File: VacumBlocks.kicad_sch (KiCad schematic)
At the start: 8 parts, among them M1 Motor_Servo, M2 Motor_Servo, M4 Motor_Servo, U2 Nodemcu-32S

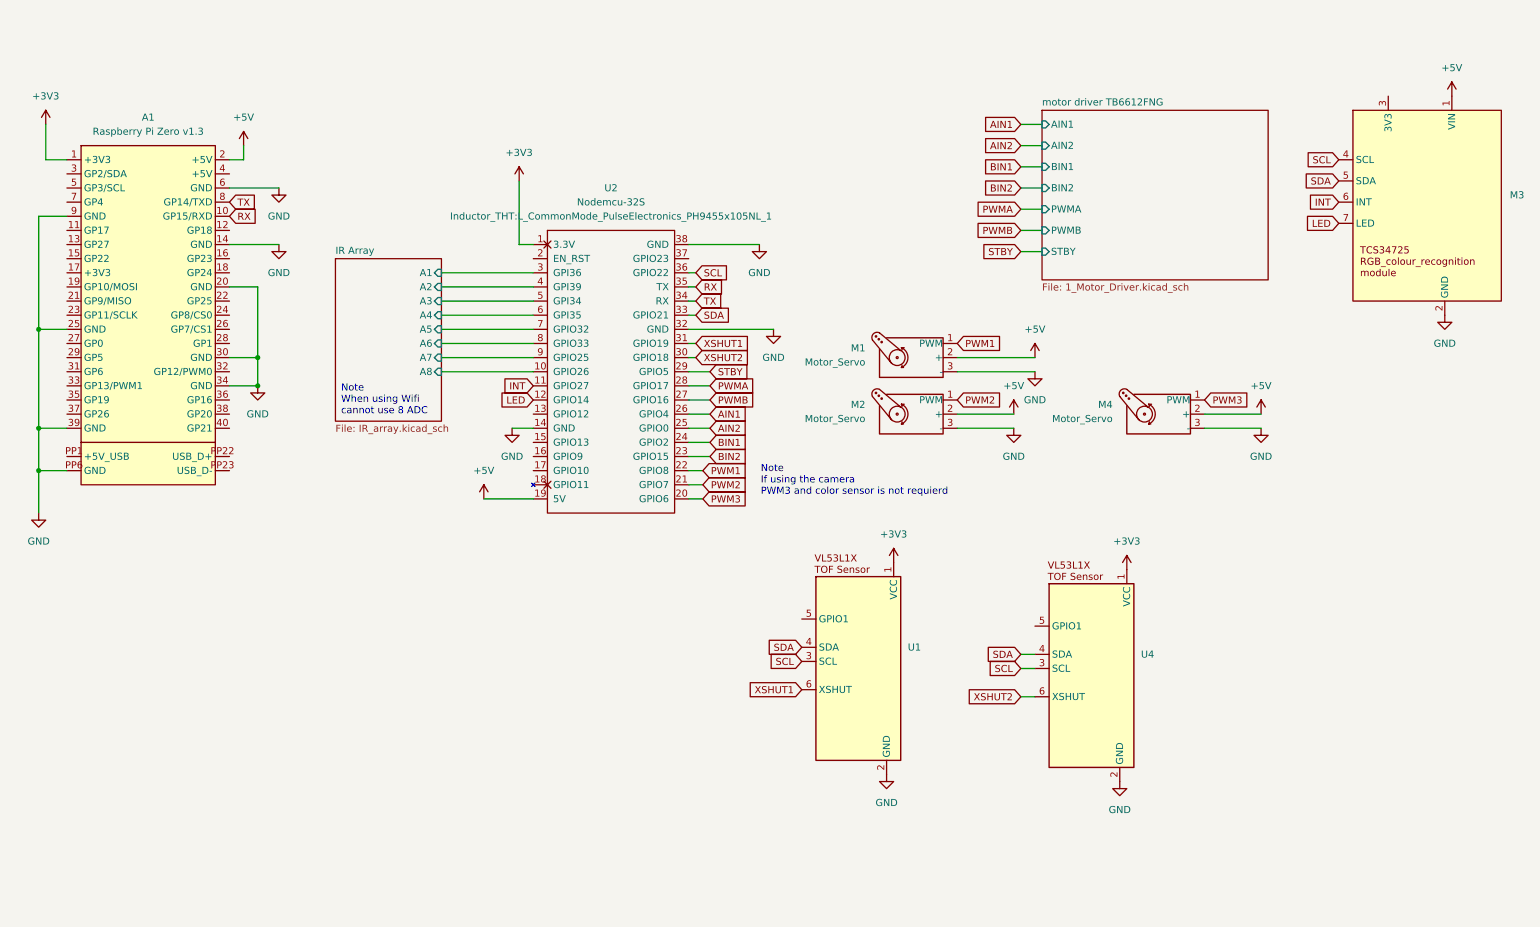
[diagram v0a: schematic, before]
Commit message: Finalized Scematics and Footprint
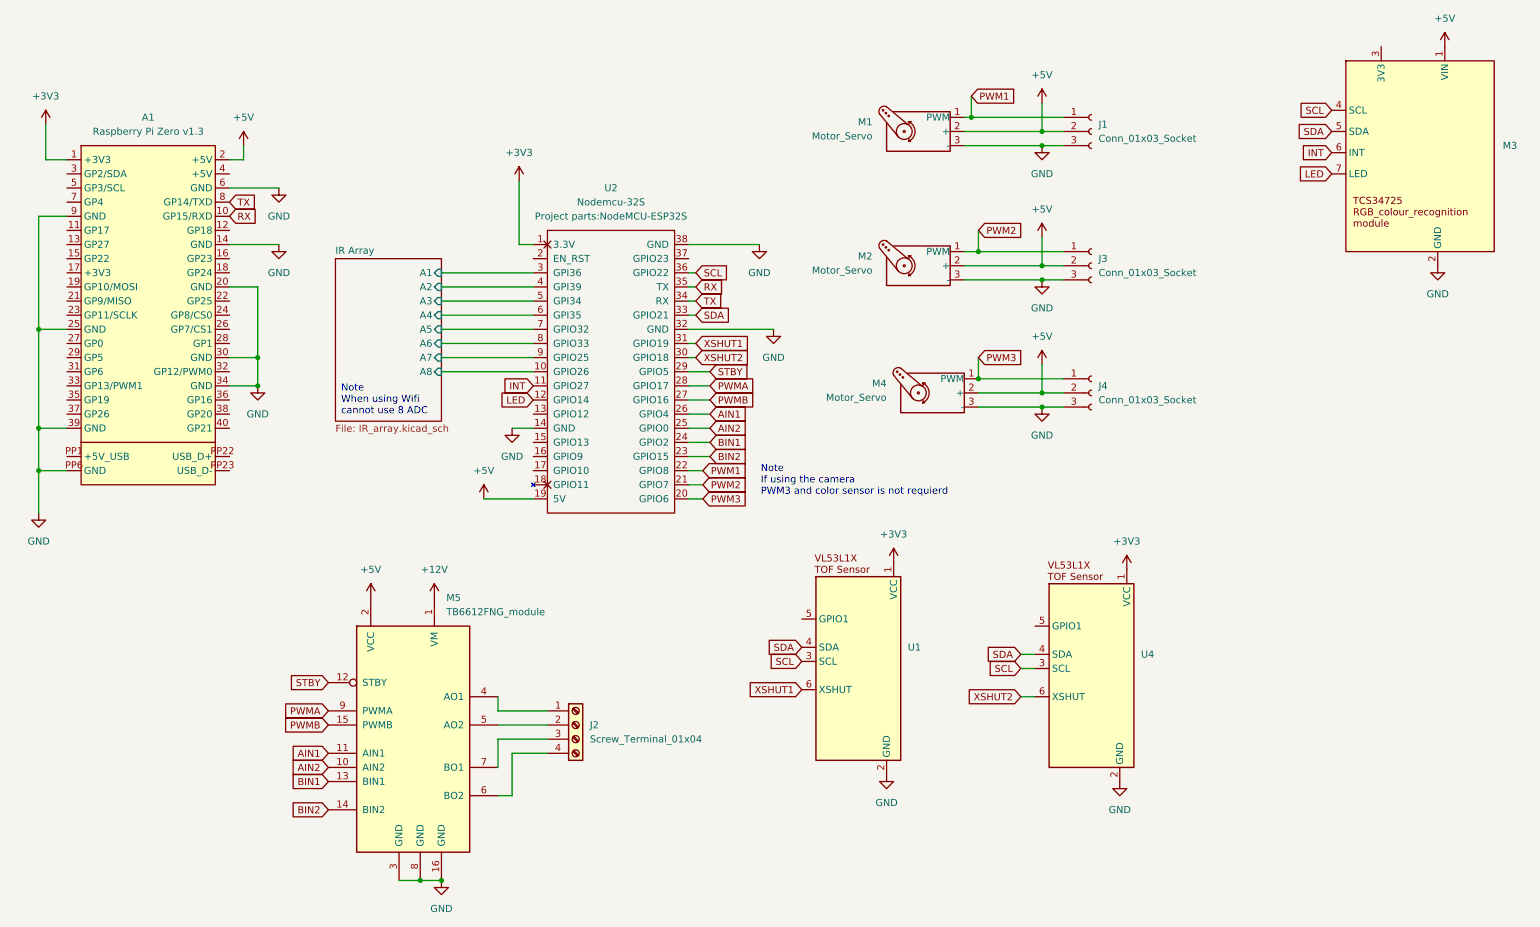
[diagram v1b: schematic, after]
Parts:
- added J1, J3, J4: Conn_01x03_Socket, Connector_PinHeader_2.54mm:PinHeader_1x03_P2.54mm_Vertical, symbol Connector:Conn_01x03_Socket
- added J2: Screw_Terminal_01x04, TerminalBlock:TerminalBlock_MaiXu_MX126-5.0-04P_1x04_P5.00mm, symbol Connector:Screw_Terminal_01x04
- added M5: TB6612FNG_module, Project parts:TB6612FNG_module, symbol Project lib:TB6612FNG_module
- A1: footprint Raspberry_Pi_Zero_v.1.3_Hat:RASPI_ZERO_FULL -> Project parts:RASPI_ZERO_FULL
- M3: footprint (none) -> Project parts:TCS34725_RGB_module
- U1, U4: footprint Sensor_Distance:ST_VL53L1x -> Project parts:VL53L0XV2 TOF Sensor moule
- U2: footprint Inductor_THT:L_CommonMode_PulseElectronics_PH9455x105NL_1 -> Project parts:NodeMCU-ESP32S
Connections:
- net +5V: now also J1.2 (Pin_2), J3.2 (Pin_2), J4.2 (Pin_2), M5.2 (VCC)
- net AIN1: now also M5.11 (AIN1)
- net AIN2: now also M5.10 (AIN2)
- net BIN1: now also M5.13 (BIN1)
- net BIN2: now also M5.14 (BIN2)
- net GND: now also J1.3 (Pin_3), J3.3 (Pin_3), J4.3 (Pin_3), M5.16 (GND), M5.3 (GND), M5.8 (GND)
- net PWM1: now also J1.1 (Pin_1)
- net PWM2: now also J3.1 (Pin_1)
- net PWM3: now also J4.1 (Pin_1)
- net PWMA: now also M5.9 (PWMA)
- net PWMB: now also M5.15 (PWMB)
- net STBY: now also M5.12 (STBY)
- new net: J2.1 (Pin_1), M5.4 (AO1)
- new net: J2.2 (Pin_2), M5.5 (AO2)
- new net: J2.4 (Pin_4), M5.6 (BO2)
- new net: J2.3 (Pin_3), M5.7 (BO1)
- new net +12V: M5.1 (VM)
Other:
- removed sheet motor driver TB6612FNG
- moved on the sheet: M1, M2, M3, M4

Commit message: Adding of the screw terminal block and schematics PDF
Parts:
- added J5: Screw_Terminal_01x03, TerminalBlock:TerminalBlock_MaiXu_MX126-5.0-03P_1x03_P5.00mm, symbol Connector:Screw_Terminal_01x03
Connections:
- net +12V: now also J5.1 (Pin_1)
- net +5V: now also J5.2 (Pin_2)
- net GND: now also J5.3 (Pin_3)
